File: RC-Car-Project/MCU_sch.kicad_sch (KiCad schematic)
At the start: 16 parts, among them SW1 SW_Push, U7 STM32H743VGTx, Y1 Crystal

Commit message: Fixed Annotations
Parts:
- C20: renamed from C35; footprint Capacitor_SMD:C_0201_0603Metric -> Capacitor_SMD:C_0603_1608Metric
- C21: renamed from C36; footprint Capacitor_SMD:C_0201_0603Metric -> Capacitor_SMD:C_0603_1608Metric
- C22: renamed from C34; footprint Capacitor_SMD:C_0201_0603Metric -> Capacitor_SMD:C_0603_1608Metric
- C23: renamed from C21; footprint Capacitor_SMD:C_0201_0603Metric -> Capacitor_SMD:C_0603_1608Metric
- C24: renamed from C40; footprint Capacitor_SMD:C_0201_0603Metric -> Capacitor_SMD:C_0603_1608Metric
- C25: renamed from C7; footprint Capacitor_SMD:C_0201_0603Metric -> Capacitor_SMD:C_0603_1608Metric
- C26: renamed from C8; footprint Capacitor_SMD:C_0201_0603Metric -> Capacitor_SMD:C_0603_1608Metric
- C27: renamed from C9; footprint Capacitor_SMD:C_0201_0603Metric -> Capacitor_SMD:C_0603_1608Metric
- C28: renamed from C10; footprint Capacitor_SMD:C_0201_0603Metric -> Capacitor_SMD:C_0603_1608Metric
- C29: renamed from C11; footprint Capacitor_SMD:C_0201_0603Metric -> Capacitor_SMD:C_0603_1608Metric
- C30: renamed from C12; footprint Capacitor_SMD:C_0201_0603Metric -> Capacitor_SMD:C_0603_1608Metric
- R14: renamed from R12; footprint Resistor_SMD:R_0201_0603Metric -> Resistor_SMD:R_0603_1608Metric
- R15: renamed from R11; footprint Resistor_SMD:R_0201_0603Metric -> Resistor_SMD:R_0603_1608Metric
- renumbered U7 to U3
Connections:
- net SWDIO: now also U3.72 (PA13); no longer U3.77 (PA15)

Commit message: Change button footprint
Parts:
- SW1: footprint Button_Switch_THT:SW_SPST_Omron_B3F-40xx -> Button_Switch_THT:SW_PUSH_6mm
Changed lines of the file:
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@@
 			)
 		)
-		(property "Footprint" "Button_Switch_THT:SW_SPST_Omron_B3F-40xx"
+		(property "Footprint" "Button_Switch_THT:SW_PUSH_6mm"
 			(at 59.69 83.82 0)
 			(effects

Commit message: Added functionality to the STM32 on the tank PCB
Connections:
- net SPI4_MOSI_RF is gone; now on net DCMI_D7: U3.5 (PE6)
- net DCMI_D2: now also U3.97 (PE0); no longer U3.65 (PC8)
- net DCMI_D3: now also U3.98 (PE1); no longer U3.66 (PC9)
- net DCMI_D7: no longer U3.96 (PB9)
- net SPI2_CS_ISENSE: now also U3.9 (PC15); no longer U3.18 (PC3_C)
- net MCU_USB_D-: now reaches U3.70 (PA11)
- net MCU_USB_D+: now reaches U3.71 (PA12)
- net SDMMC1_D2: now reaches U3.78 (PC10)
- net SDMMC1_D3: now reaches U3.79 (PC11)
- net SPI2_CS_ADC: now reaches U3.8 (PC14)
- net SDMMC1_CK: now reaches U3.80 (PC12)
- net RF_RESET: now reaches U3.81 (PD0)
- net SDMMC1_CMD: now reaches U3.83 (PD2)
- net I2C2_CAM_SCL renamed I2C2_SCL
- net I2C2_CAM_SDA renamed I2C2_SDA
- net RF_NRST: no longer names the net of U3.40 (PE10)
- net SPI2_MISO_ISENSE renamed SPI2_MISO
- net SPI2_MOSI_ISENSE renamed SPI2_MOSI
- net SPI2_SCLK_ISENSE renamed SPI2_CLK
- net SPI4_CS_RF: no longer names the net of U3.41 (PE11)
- net SPI4_MISO_RF: no longer names the net of U3.43 (PE13)
- net SPI4_SCLK_RF: no longer names the net of U3.42 (PE12)
- net THERM_ADC_CS: no longer names the net of U3.32 (PC4)
- new net SDMMC1_D0: U3.65 (PC8)
- new net SDMMC1_D1: U3.66 (PC9)
- no-connect marks 44 -> 39
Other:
- note added: "XCLK may need to be generated with SW"

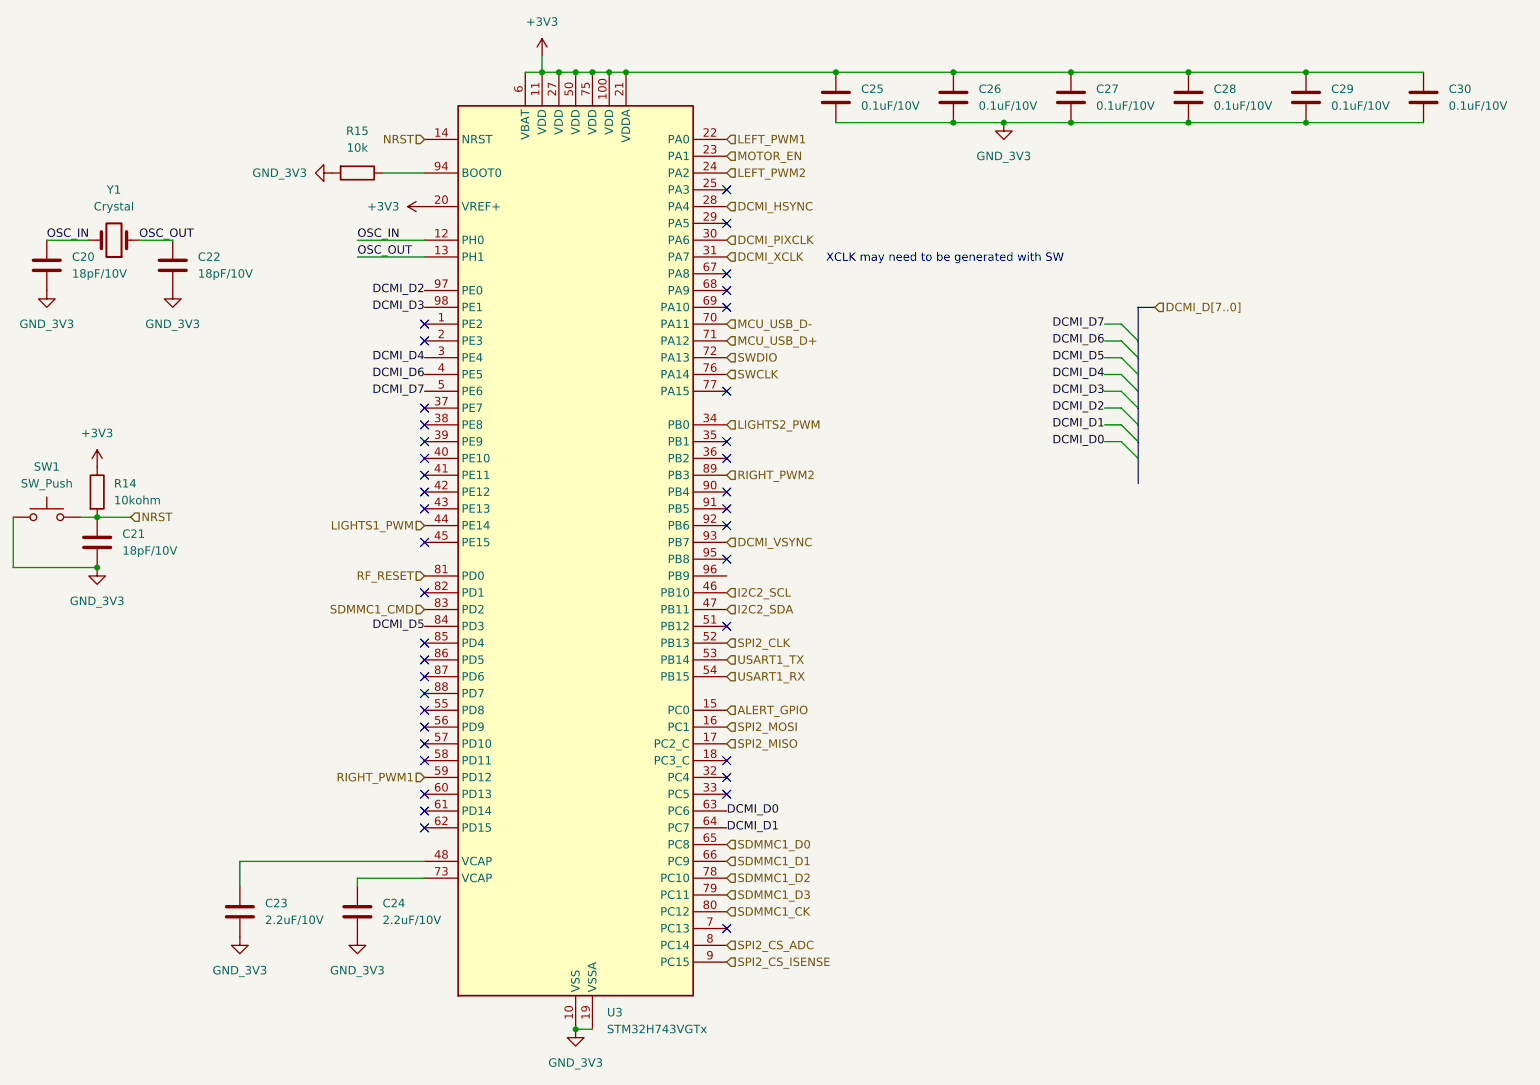
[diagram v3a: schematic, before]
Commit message: Finished prelim. Car and added screw holes
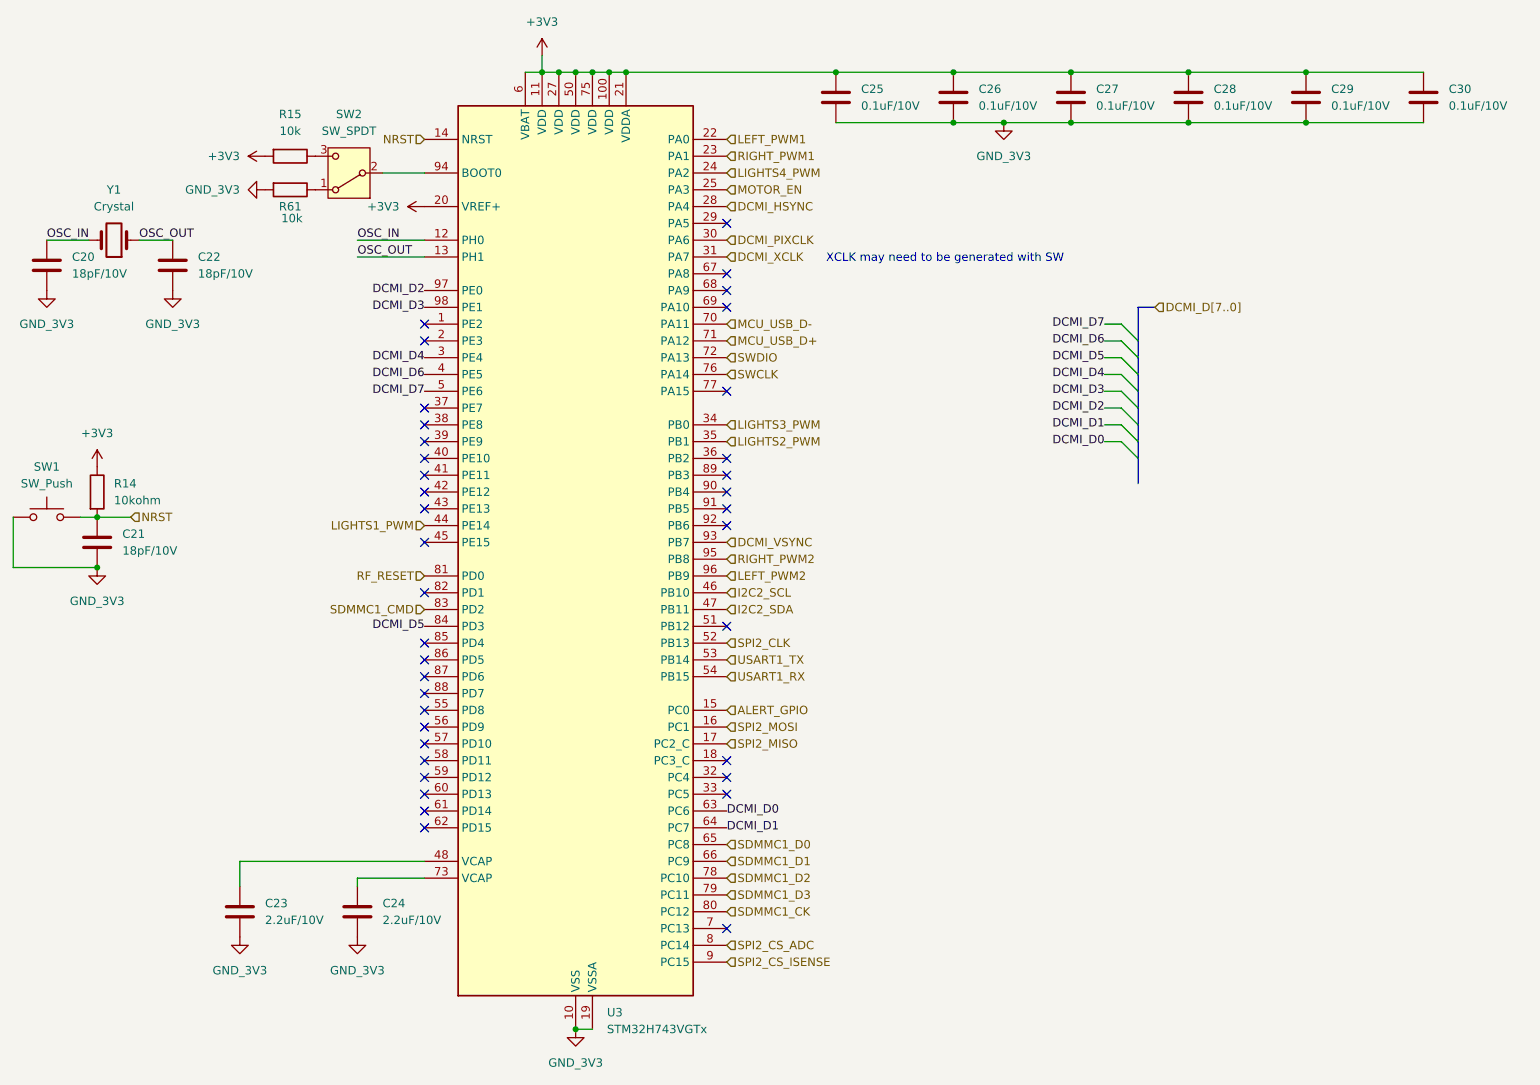
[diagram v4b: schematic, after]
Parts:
- added R61: 10k, Capacitor_SMD:C_0603_1608Metric, symbol Device:R
- added SW2: SW_SPDT, Connector_PinHeader_2.54mm:PinHeader_1x03_P2.54mm_Vertical, symbol Switch:SW_SPDT
- R15: footprint Resistor_SMD:R_0603_1608Metric -> Capacitor_SMD:C_0603_1608Metric
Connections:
- net +3V3: now also R15.2
- net GND_3V3: now also R61.2; no longer R15.2
- net LEFT_PWM2: now also U3.96 (PB9); no longer U3.24 (PA2)
- net LIGHTS2_PWM: now also U3.35 (PB1); no longer U3.34 (PB0)
- net MOTOR_EN: now also U3.25 (PA3); no longer U3.23 (PA1)
- net RIGHT_PWM1: now also U3.23 (PA1); no longer U3.59 (PD12)
- net RIGHT_PWM2: now also U3.95 (PB8); no longer U3.89 (PB3)
- net at U3.94 (BOOT0): now also SW2.2 (B); no longer R15.1
- new net: R61.1, SW2.1 (A)
- new net: R15.1, SW2.3 (C)
- new net LIGHTS3_PWM: U3.34 (PB0)
- new net LIGHTS4_PWM: U3.24 (PA2)
- no-connect marks 39 -> 38

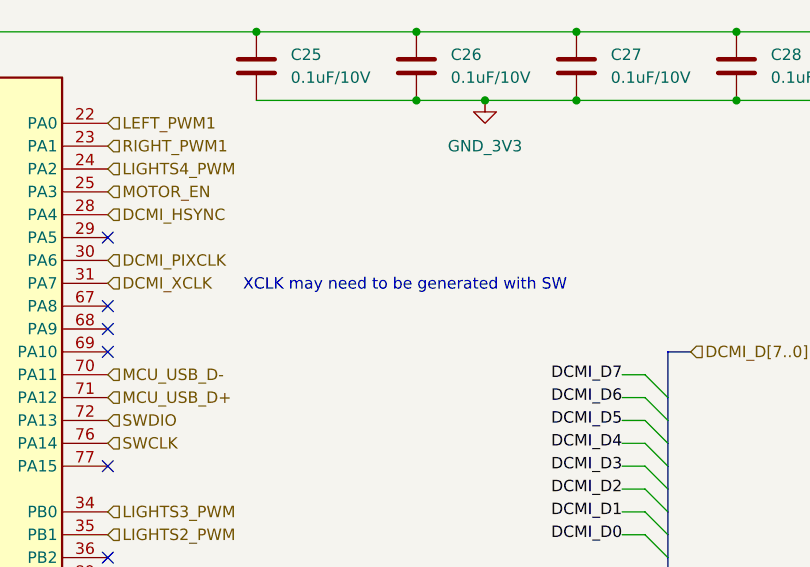
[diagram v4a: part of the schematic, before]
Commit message: Updated STM32Cube Schem
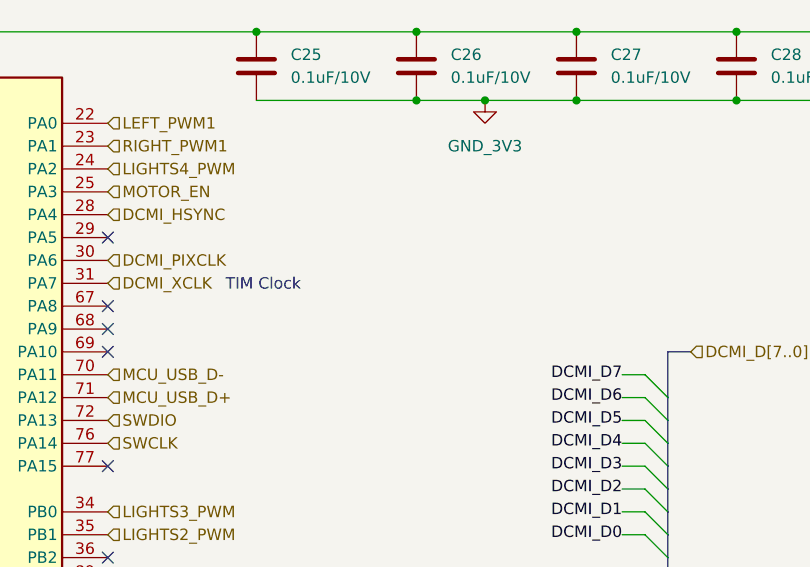
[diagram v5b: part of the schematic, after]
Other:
- note added: "TIM Clock"
- note removed: "XCLK may need to be generated with SW"
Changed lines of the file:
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@@
 		)
 	)
-	(text "XCLK may need to be generated with SW"
+	(text "TIM Clock"
 		(exclude_from_sim no)
-		(at 195.58 49.784 0)
+		(at 179.832 49.784 0)
 		(effects
 			(font

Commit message: Fixed Resistors
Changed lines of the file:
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@@
 		)
 		(property "Value" "10k"
-			(at 96.774 43.688 90)
+			(at 96.52 44.45 90)
 			(effects
 				(font
@@
 		(on_board yes)
 		(dnp no)
-		(fields_autoplaced yes)
 		(property "Reference" "R15"
-			(at 96.52 27.94 90)
+			(at 96.52 29.718 90)
 			(effects
 				(font
@@
 		)
 		(property "Value" "10k"
-			(at 96.52 30.48 90)
-			(effects
-				(font
+			(at 96.52 32.004 90)
+			(effects
+				(font

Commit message: Resistor manuf PNs labelled
resistor manufacturer part numbers added
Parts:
- R14, R15, R61: MANUF_PN (none) -> RC0603FR-0710KL
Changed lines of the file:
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@@
 			)
 		)
-		(property "MANUF_PN" ""
+		(property "MANUF_PN" "RC0603FR-0710KL"
 			(at 67.31 85.09 0)
 			(effects
@@
 			)
 		)
-		(property "MANUF_PN" ""
+		(property "MANUF_PN" "RC0603FR-0710KL"
 			(at 96.52 39.37 0)
 			(effects
@@
 			)
 		)
-		(property "MANUF_PN" ""
+		(property "MANUF_PN" "RC0603FR-0710KL"
 			(at 96.52 34.29 0)
 			(effects
